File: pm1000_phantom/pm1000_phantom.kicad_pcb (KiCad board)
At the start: 2 copper layers, 27 x 44.5 mm, 17 parts, among them J1 2 pin 2,54mm Molex, J10 2 pin 2,54mm Molex, J2 2 pin 2,54mm Molex, J3 2 pin 2,54mm Molex, J4 2 pin 2,54mm Molex, J5 2 pin 2,54mm Molex, J6 3 pin 2,54mm Molex, J7 3 pin 2,54mm Molex, J8 3 pin 2,54mm Molex, J9 3 pin 2,54mm Molex

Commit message: fix phantom board labels
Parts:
- J1: value 2 pin 2,54mm Molex -> Bla
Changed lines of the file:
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@@
 		(property "Value" "3 pin 2,54mm Molex"
 			(at 2.54 4.08 90)
-			(layer "F.Fab")
-			(hide yes)
+			(layer "F.SilkS")
 			(effects
 				(font
@@
 		(property "Value" "2 pin 2,54mm Molex"
 			(at 1.27 4.08 0)
-			(layer "F.Fab")
-			(hide yes)
+			(layer "F.SilkS")
 			(effects
 				(font
@@
 			)
 		)
-		(property "Value" "2 pin 2,54mm Molex"
+		(property "Value" "Bla"
 			(at 1.27 4.08 0)
-			(layer "F.Fab")
-			(hide yes)
+			(layer "F.SilkS")
 			(effects
 				(font
@@
 			(at -2.54 3.81 0)
 			(layer "F.Fab")
-			(hide yes)
 			(effects
 				(font
@@
 			(at -0.485 2.41 0)
 			(layer "F.SilkS")
+			(hide yes)
 			(effects
 				(font
@@
 		(property "Value" "2 pin 2,54mm Molex"
 			(at 1.27 4.08 90)
-			(layer "F.Fab")
+			(layer "F.SilkS")
 			(effects
 				(font
@@
 		(property "Value" "2 pin 2,54mm Molex"
 			(at 1.27 4.08 90)
-			(layer "F.Fab")
-			(hide yes)
+			(layer "F.SilkS")
 			(effects
 				(font

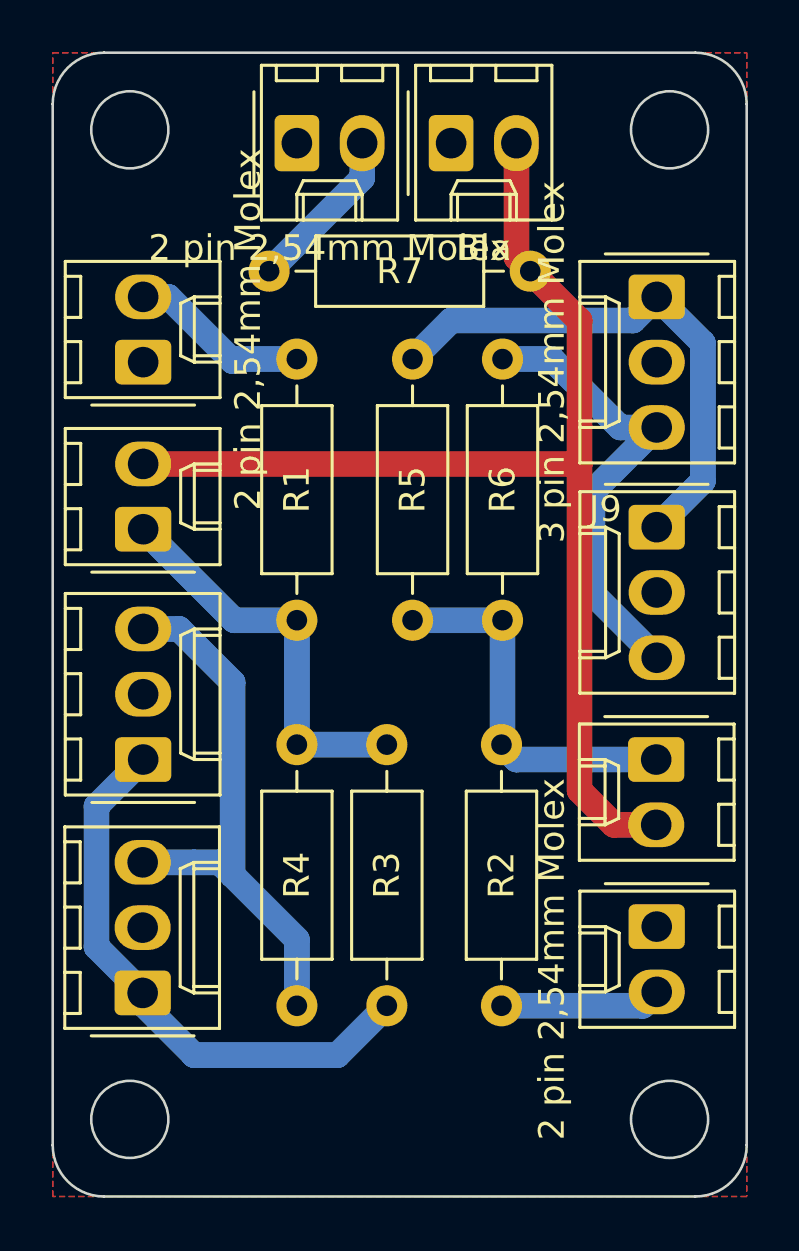
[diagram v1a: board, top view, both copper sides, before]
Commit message: phantom board connector descriptions
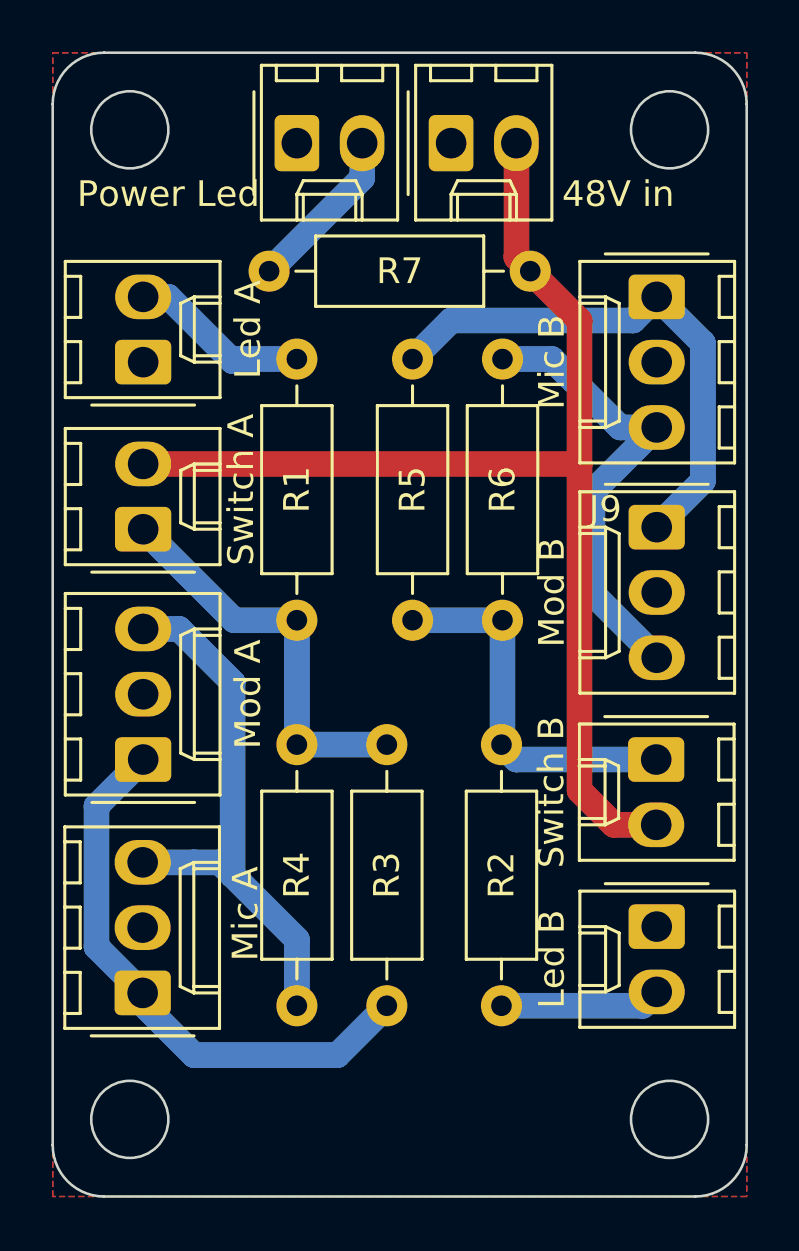
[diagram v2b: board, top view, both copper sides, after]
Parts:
- J1: value Bla -> 48V in
- J10: value 2 pin 2,54mm Molex -> Power Led
- J2: value 2 pin 2,54mm Molex -> Switch A
- J3: value 2 pin 2,54mm Molex -> Switch B
- J4: value 2 pin 2,54mm Molex -> Led A
- J5: value 2 pin 2,54mm Molex -> Led B
- J6: value 3 pin 2,54mm Molex -> Mic A
- J7: value 3 pin 2,54mm Molex -> Mod A
- J8: value 3 pin 2,54mm Molex -> Mic B
- J9: value 3 pin 2,54mm Molex -> Mod B
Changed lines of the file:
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@@
 			)
 		)
-		(property "Value" "3 pin 2,54mm Molex"
-			(at 2.54 4.08 90)
-			(layer "F.Fab")
-			(hide yes)
+		(property "Value" "Mic A"
+			(at 3.08 4 90)
+			(layer "F.SilkS")
 			(effects
 				(font
@@
 			)
 		)
-		(property "Value" "3 pin 2,54mm Molex"
+		(property "Value" "Mic B"
 			(at 2.54 4.08 90)
 			(layer "F.SilkS")
@@
 			)
 		)
-		(property "Value" "2 pin 2,54mm Molex"
-			(at 1.27 4.08 0)
+		(property "Value" "Power Led"
+			(at -5 1.98 0)
 			(layer "F.SilkS")
 			(effects
@@
 			)
 		)
-		(property "Value" "Bla"
-			(at 1.27 4.08 0)
+		(property "Value" "48V in"
+			(at 6.5 1.98 0)
 			(layer "F.SilkS")
 			(effects
@@
 			)
 		)
-		(property "Value" "3 pin 2,54mm Molex"
+		(property "Value" "Mod B"
 			(at 2.54 4.08 90)
-			(layer "F.Fab")
+			(layer "F.SilkS")
 			(effects
 				(font
@@
 		)
 		(property "Datasheet" "~"
-			(at 0 0 270)
+			(at 0 0 90)
 			(layer "F.Fab")
 			(hide yes)
@@
 		)
 		(property "Description" ""
-			(at 0 0 270)
+			(at 0 0 90)
 			(layer "F.Fab")
 			(hide yes)
@@
 			)
 		)
-		(property "Value" "2 pin 2,54mm Molex"
+		(property "Value" "Switch B"
 			(at 1.27 4.08 90)
-			(layer "F.Fab")
-			(hide yes)
+			(layer "F.SilkS")
 			(effects
 				(font
@@
 			)
 		)
-		(property "Value" "2 pin 2,54mm Molex"
-			(at -2.54 3.81 0)
-			(layer "F.Fab")
+		(property "Value" "Switch A"
+			(at 1.54 3.81 90)
+			(layer "F.SilkS")
 			(effects
 				(font
@@
 			)
 		)
-		(property "Value" "2 pin 2,54mm Molex"
-			(at 1.27 4.08 90)
+		(property "Value" "Led A"
+			(at 1.27 4.08 270)
 			(layer "F.SilkS")
 			(effects
@@
 			)
 		)
-		(property "Value" "3 pin 2,54mm Molex"
+		(property "Value" "Mod A"
 			(at 2.54 4.08 90)
-			(layer "F.Fab")
-			(hide yes)
+			(layer "F.SilkS")
 			(effects
 				(font
@@
 			)
 		)
-		(property "Value" "2 pin 2,54mm Molex"
+		(property "Value" "Led B"
 			(at 1.27 4.08 90)
 			(layer "F.SilkS")
